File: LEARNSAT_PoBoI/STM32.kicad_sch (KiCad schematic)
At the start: 24 parts, among them U17 LP5907SNX-3.3, U21 74AC14MTCX, U22 LTC4304CMS#PBF, U26 ISL3259EIRZ, U6 STM32F103RET6, Y1 ABS07-166-32.768KHZ-T

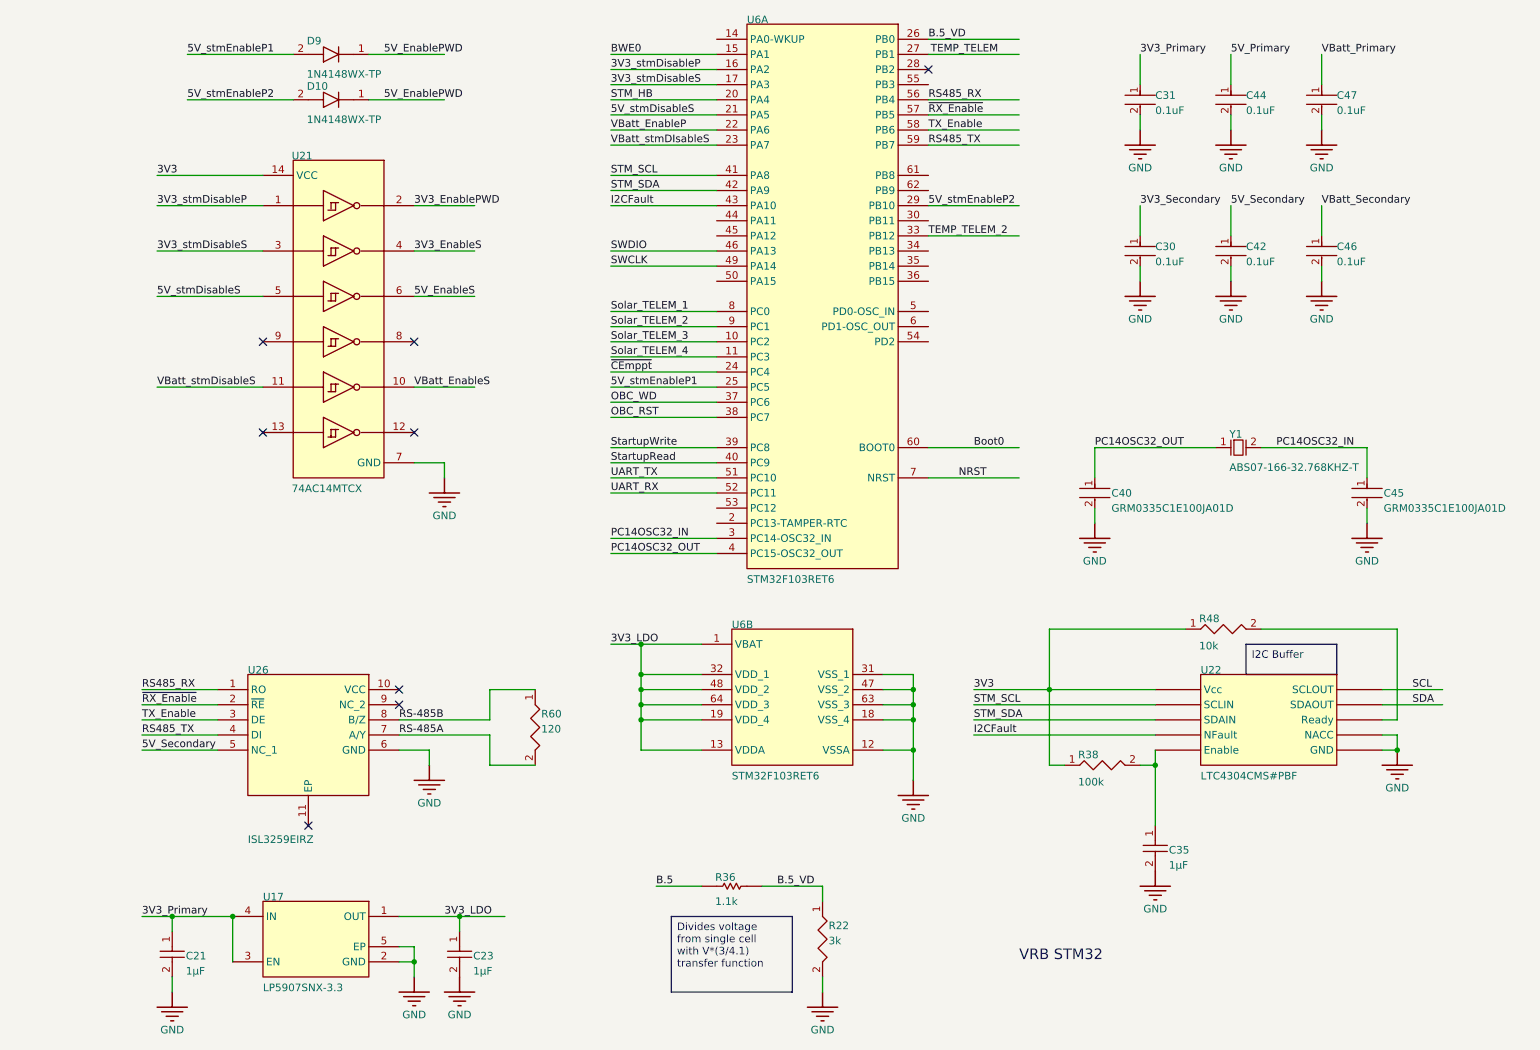
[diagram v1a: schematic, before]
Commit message: Replaced local nets with global and left local nets intact
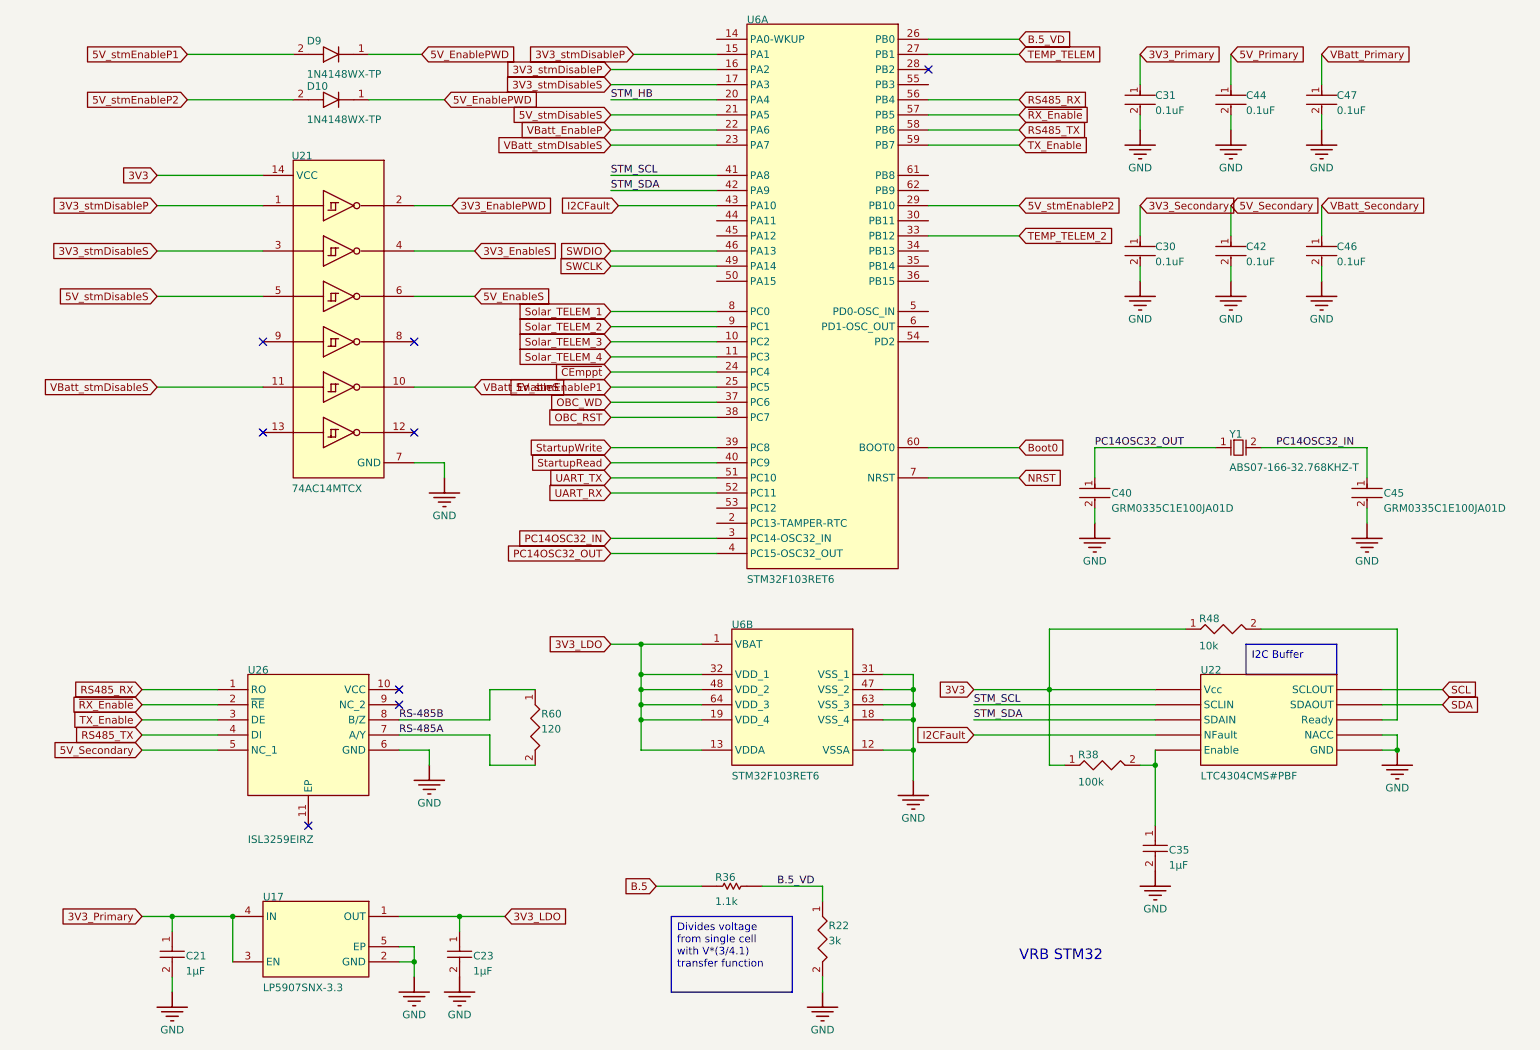
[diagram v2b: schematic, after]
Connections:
- net BWE0 is gone; now on net 3V3_stmDisableP: U6.15 (PA1)
- net RS485_TX: now also U6.58 (PB6); no longer U6.59 (PB7)
- net TX_Enable: now also U6.59 (PB7); no longer U6.58 (PB6)

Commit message: Added footprints
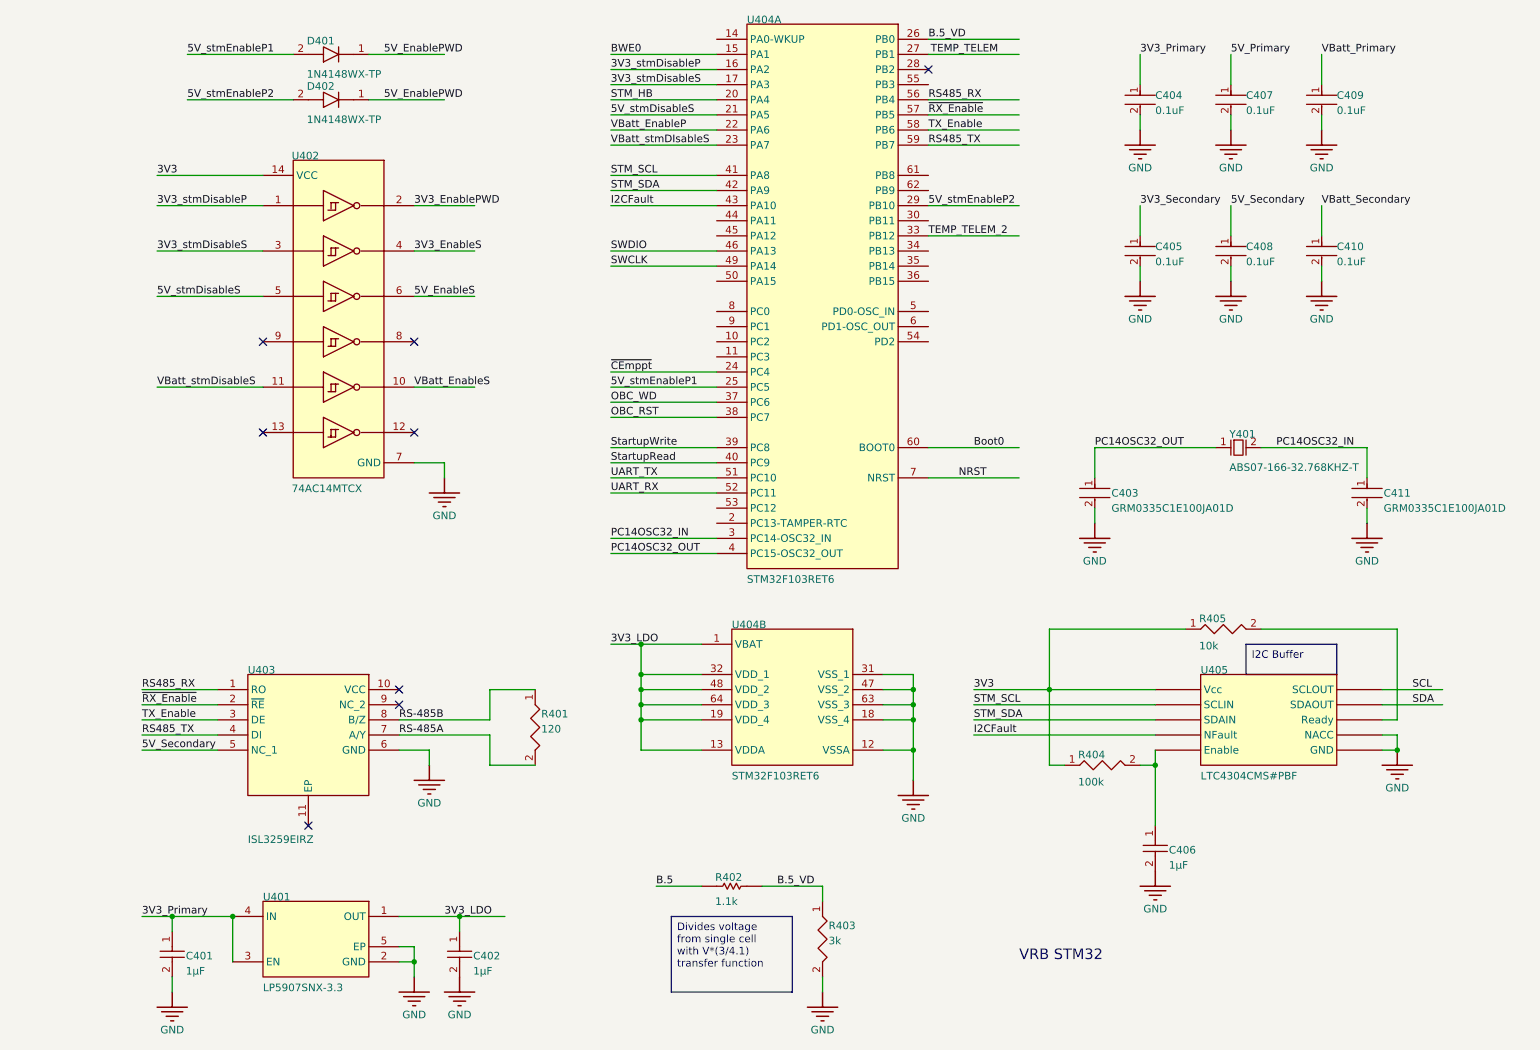
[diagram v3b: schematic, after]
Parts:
- C401: renamed from C21; footprint FP-CC0201-BA-IPC_A -> Capacitor_SMD:C_0201_0603Metric
- C402: renamed from C23; footprint FP-CC0201-BA-IPC_A -> Capacitor_SMD:C_0201_0603Metric
- C403: renamed from C40; footprint FP-GRM033-0_03-IPC_A -> Capacitor_SMD:C_0201_0603Metric
- C404: renamed from C31; footprint FP-C0603-CJ-MFG -> Capacitor_SMD:C_0603_1608Metric
- C405: renamed from C30; footprint FP-C0603-CJ-MFG -> Capacitor_SMD:C_0603_1608Metric
- C406: renamed from C35; footprint CAPC1608X94X35NL15T15 -> Capacitor_SMD:C_0603_1608Metric
- C407: renamed from C44; footprint FP-C0603-CJ-MFG -> Capacitor_SMD:C_0603_1608Metric
- C408: renamed from C42; footprint FP-C0603-CJ-MFG -> Capacitor_SMD:C_0603_1608Metric
- C409: renamed from C47; footprint FP-C0603-CJ-MFG -> Capacitor_SMD:C_0603_1608Metric
- C410: renamed from C46; footprint FP-C0603-CJ-MFG -> Capacitor_SMD:C_0603_1608Metric
- C411: renamed from C45; footprint FP-GRM033-0_03-IPC_A -> Capacitor_SMD:C_0201_0603Metric
- D401: renamed from D9; footprint 1N4148WX-TP-Footprint-1 -> Diode_SMD:D_SOD-323
- D402: renamed from D10; footprint 1N4148WX-TP-Footprint-1 -> Diode_SMD:D_SOD-323
- R401: renamed from R60; footprint RESC0603(1608)_L -> Resistor_SMD:R_0603_1608Metric
- R402: renamed from R36; footprint RESC1005X40X25NL05T10 -> Resistor_SMD:R_0402_1005Metric
- R403: renamed from R22; footprint RESC0402(1005)_L -> Resistor_SMD:R_0402_1005Metric
- R404: renamed from R38; footprint RESC3216X60X45ML15T20 -> Resistor_SMD:R_1206_3216Metric
- R405: renamed from R48; footprint RESC1608X55X25ML10T15 -> Resistor_SMD:R_0603_1608Metric
- U401: renamed from U17; footprint TI-DQN4-480X480TP_V -> LP5907SNX-3.3:IC_TPS7A0230PDQNR
- U402: renamed from U21; footprint FP-948G-MFG -> 74AC14MTCX:SOP65P640X120-14N
- U403: renamed from U26; footprint ISL3259EIRZ-Footprint-1 -> ISL3259EIRZ-T:SON50P300X300X100-11N
- U404: renamed from U6; footprint STM-LQFP64_N -> KiCad:QFP50P1200X1200X160-64N
- U405: renamed from U22; footprint LTC4304CMS#PBF-Footprint-1 -> LTC4304CMS_PBF:MSOP-10_MS
- Y401: renamed from Y1; footprint EPSON-FC-135_V -> ABS07-166-32.768KHZ-T:XTAL_ABS07-166-32.768KHZ-T
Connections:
- net 3V3_stmDisableP: no longer U404.15 (PA1)
- net RS485_TX: now also U404.59 (PB7); no longer U404.58 (PB6)
- net TX_Enable: now also U404.58 (PB6); no longer U404.59 (PB7)
- net Solar_TELEM_1: no longer names the net of U404.8 (PC0)
- net Solar_TELEM_2: no longer names the net of U404.9 (PC1)
- net Solar_TELEM_3: no longer names the net of U404.10 (PC2)
- net Solar_TELEM_4: no longer names the net of U404.11 (PC3)
- new net BWE0: U404.15 (PA1)

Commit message: Add files via upload
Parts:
- C21: renamed from C401; footprint Capacitor_SMD:C_0201_0603Metric -> FP-CC0201-BA-IPC_A
- C23: renamed from C402; footprint Capacitor_SMD:C_0201_0603Metric -> FP-CC0201-BA-IPC_A
- C30: renamed from C405; footprint Capacitor_SMD:C_0603_1608Metric -> FP-C0603-CJ-MFG
- C31: renamed from C404; footprint Capacitor_SMD:C_0603_1608Metric -> FP-C0603-CJ-MFG
- C35: renamed from C406; footprint Capacitor_SMD:C_0603_1608Metric -> CAPC1608X94X35NL15T15
- C40: renamed from C403; footprint Capacitor_SMD:C_0201_0603Metric -> FP-GRM033-0_03-IPC_A
- C42: renamed from C408; footprint Capacitor_SMD:C_0603_1608Metric -> FP-C0603-CJ-MFG
- C44: renamed from C407; footprint Capacitor_SMD:C_0603_1608Metric -> FP-C0603-CJ-MFG
- C45: renamed from C411; footprint Capacitor_SMD:C_0201_0603Metric -> FP-GRM033-0_03-IPC_A
- C46: renamed from C410; footprint Capacitor_SMD:C_0603_1608Metric -> FP-C0603-CJ-MFG
- C47: renamed from C409; footprint Capacitor_SMD:C_0603_1608Metric -> FP-C0603-CJ-MFG
- D10: renamed from D402; footprint Diode_SMD:D_SOD-323 -> 1N4148WX-TP-Footprint-1
- D9: renamed from D401; footprint Diode_SMD:D_SOD-323 -> 1N4148WX-TP-Footprint-1
- R22: renamed from R403; footprint Resistor_SMD:R_0402_1005Metric -> RESC0402(1005)_L
- R36: renamed from R402; footprint Resistor_SMD:R_0402_1005Metric -> RESC1005X40X25NL05T10
- R38: renamed from R404; footprint Resistor_SMD:R_1206_3216Metric -> RESC3216X60X45ML15T20
- R48: renamed from R405; footprint Resistor_SMD:R_0603_1608Metric -> RESC1608X55X25ML10T15
- R60: renamed from R401; footprint Resistor_SMD:R_0603_1608Metric -> RESC0603(1608)_L
- U17: renamed from U401; footprint LP5907SNX-3.3:IC_TPS7A0230PDQNR -> TI-DQN4-480X480TP_V
- U21: renamed from U402; footprint 74AC14MTCX:SOP65P640X120-14N -> FP-948G-MFG
- U22: renamed from U405; footprint LTC4304CMS_PBF:MSOP-10_MS -> LTC4304CMS#PBF-Footprint-1
- U26: renamed from U403; footprint ISL3259EIRZ-T:SON50P300X300X100-11N -> ISL3259EIRZ-Footprint-1
- U6: renamed from U404; footprint KiCad:QFP50P1200X1200X160-64N -> STM-LQFP64_N
- Y1: renamed from Y401; footprint ABS07-166-32.768KHZ-T:XTAL_ABS07-166-32.768KHZ-T -> EPSON-FC-135_V
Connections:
- net BWE0 is gone; now on net 3V3_stmDisableP: U6.15 (PA1)
- net RS485_TX: now also U6.58 (PB6); no longer U6.59 (PB7)
- net TX_Enable: now also U6.59 (PB7); no longer U6.58 (PB6)
- net Solar_TELEM_3: now reaches U6.10 (PC2)
- net Solar_TELEM_4: now reaches U6.11 (PC3)
- net Solar_TELEM_1: now reaches U6.8 (PC0)
- net Solar_TELEM_2: now reaches U6.9 (PC1)
